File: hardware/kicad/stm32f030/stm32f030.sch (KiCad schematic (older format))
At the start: 5 parts, among them P1 5VIN, U1 LM1117-3.3

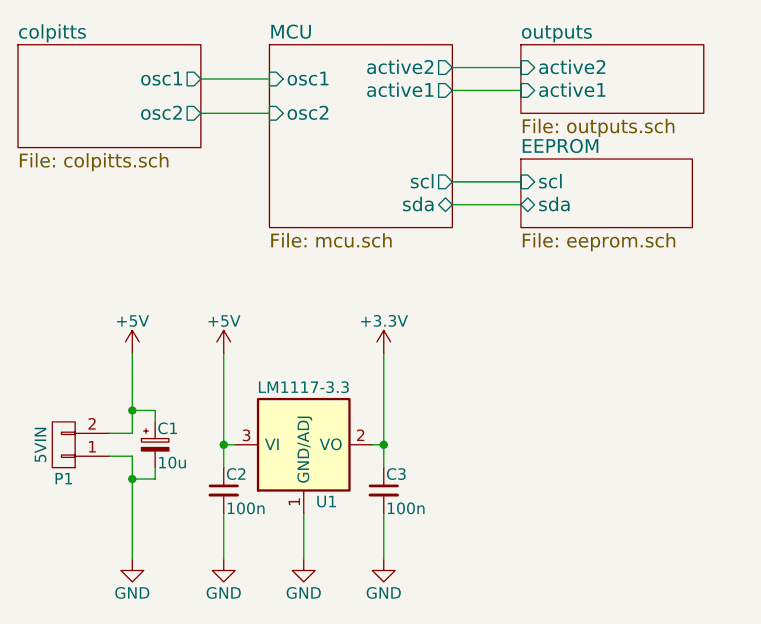
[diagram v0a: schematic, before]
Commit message: hardware/kicad/stm32f030: kicad version && lib bump
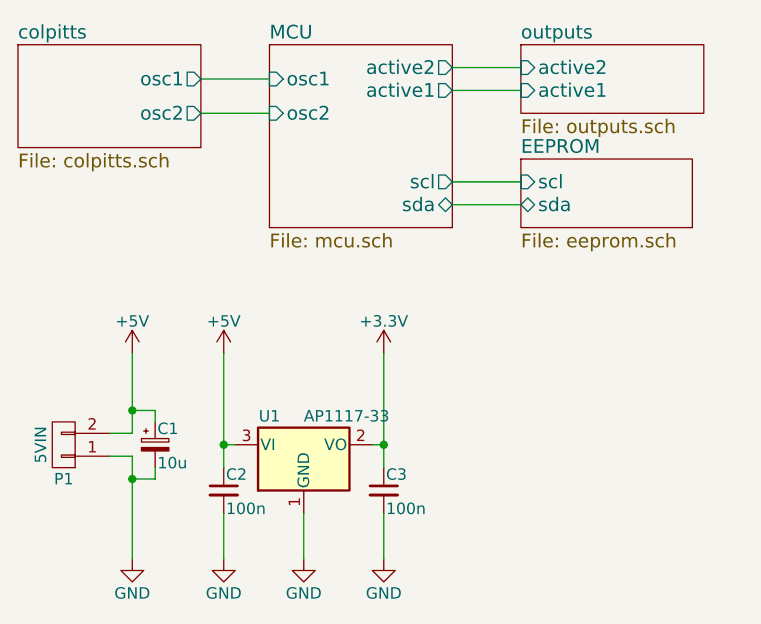
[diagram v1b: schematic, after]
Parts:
- removed U1: LM1117-3.3, TO_SOT_Packages_SMD:SOT-223, symbol LM1117-3.3
- added U1: AP1117-33, TO_SOT_Packages_SMD:SOT-223-3Lead_TabPin2, symbol AP1117-33
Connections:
- net +3V3: now also U1.2 (VO)
- net +5V: now also U1.3 (VI)
- net GND: now also U1.1 (GND)
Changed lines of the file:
@@
 LIBS:transistors
 LIBS:conn
-LIBS:linear
 LIBS:regul
-LIBS:74xx
-LIBS:cmos4000
-LIBS:adc-dac
-LIBS:memory
-LIBS:xilinx
-LIBS:microcontrollers
-LIBS:dsp
-LIBS:microchip
-LIBS:analog_switches
-LIBS:motorola
-LIBS:texas
-LIBS:intel
-LIBS:audio
-LIBS:interface
-LIBS:digital-audio
-LIBS:philips
-LIBS:display
-LIBS:cypress
-LIBS:siliconi
-LIBS:opto
-LIBS:atmel
-LIBS:contrib
-LIBS:valves
 LIBS:stm32
 LIBS:switches
@@
 $EndComp
 $Comp
-L LM1117-3.3 U1
-U 1 1 5884B3D9
-P 5750 4500
-F 0 "U1" H 5850 4250 50  0000 C CNN
-F 1 "LM1117-3.3" H 5750 4750 50  0000 C CNN
-F 2 "TO_SOT_Packages_SMD:SOT-223" H 5750 4500 50  0001 C CNN
-F 3 "" H 5750 4500 50  0000 C CNN
-	1    5750 4500
-	1    0    0    -1
-$EndComp
-$Comp
 L GND #PWR03
 U 1 1 5884B8B0
@@
 Wire Wire Line
 	5300 2900 5600 2900
+$Comp
+L AP1117-33 U1
+U 1 1 59C162EF
+P 5750 4500
+F 0 "U1" H 5600 4625 50  0000 C CNN
+F 1 "AP1117-33" H 5750 4625 50  0000 L CNN
+F 2 "TO_SOT_Packages_SMD:SOT-223-3Lead_TabPin2" H 5750 4700 50  0001 C CNN
+F 3 "" H 5850 4250 50  0001 C CNN
+	1    5750 4500
+	1    0    0    -1
+$EndComp
 $EndSCHEMATC
